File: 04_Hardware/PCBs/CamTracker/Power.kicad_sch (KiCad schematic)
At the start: 95 parts, among them IC2 AP7361E-33FGE-7, IC3 AP7361E-33FGE-7, J1 PJ-059A, J2 67996-100HLF, U1 SC206EEMDA-G51-UGNDA, U15 AP61100Z6-7, U2 AP64502QSP-13, U3 AP7335-WG-7, U6 AP61300Z6-7

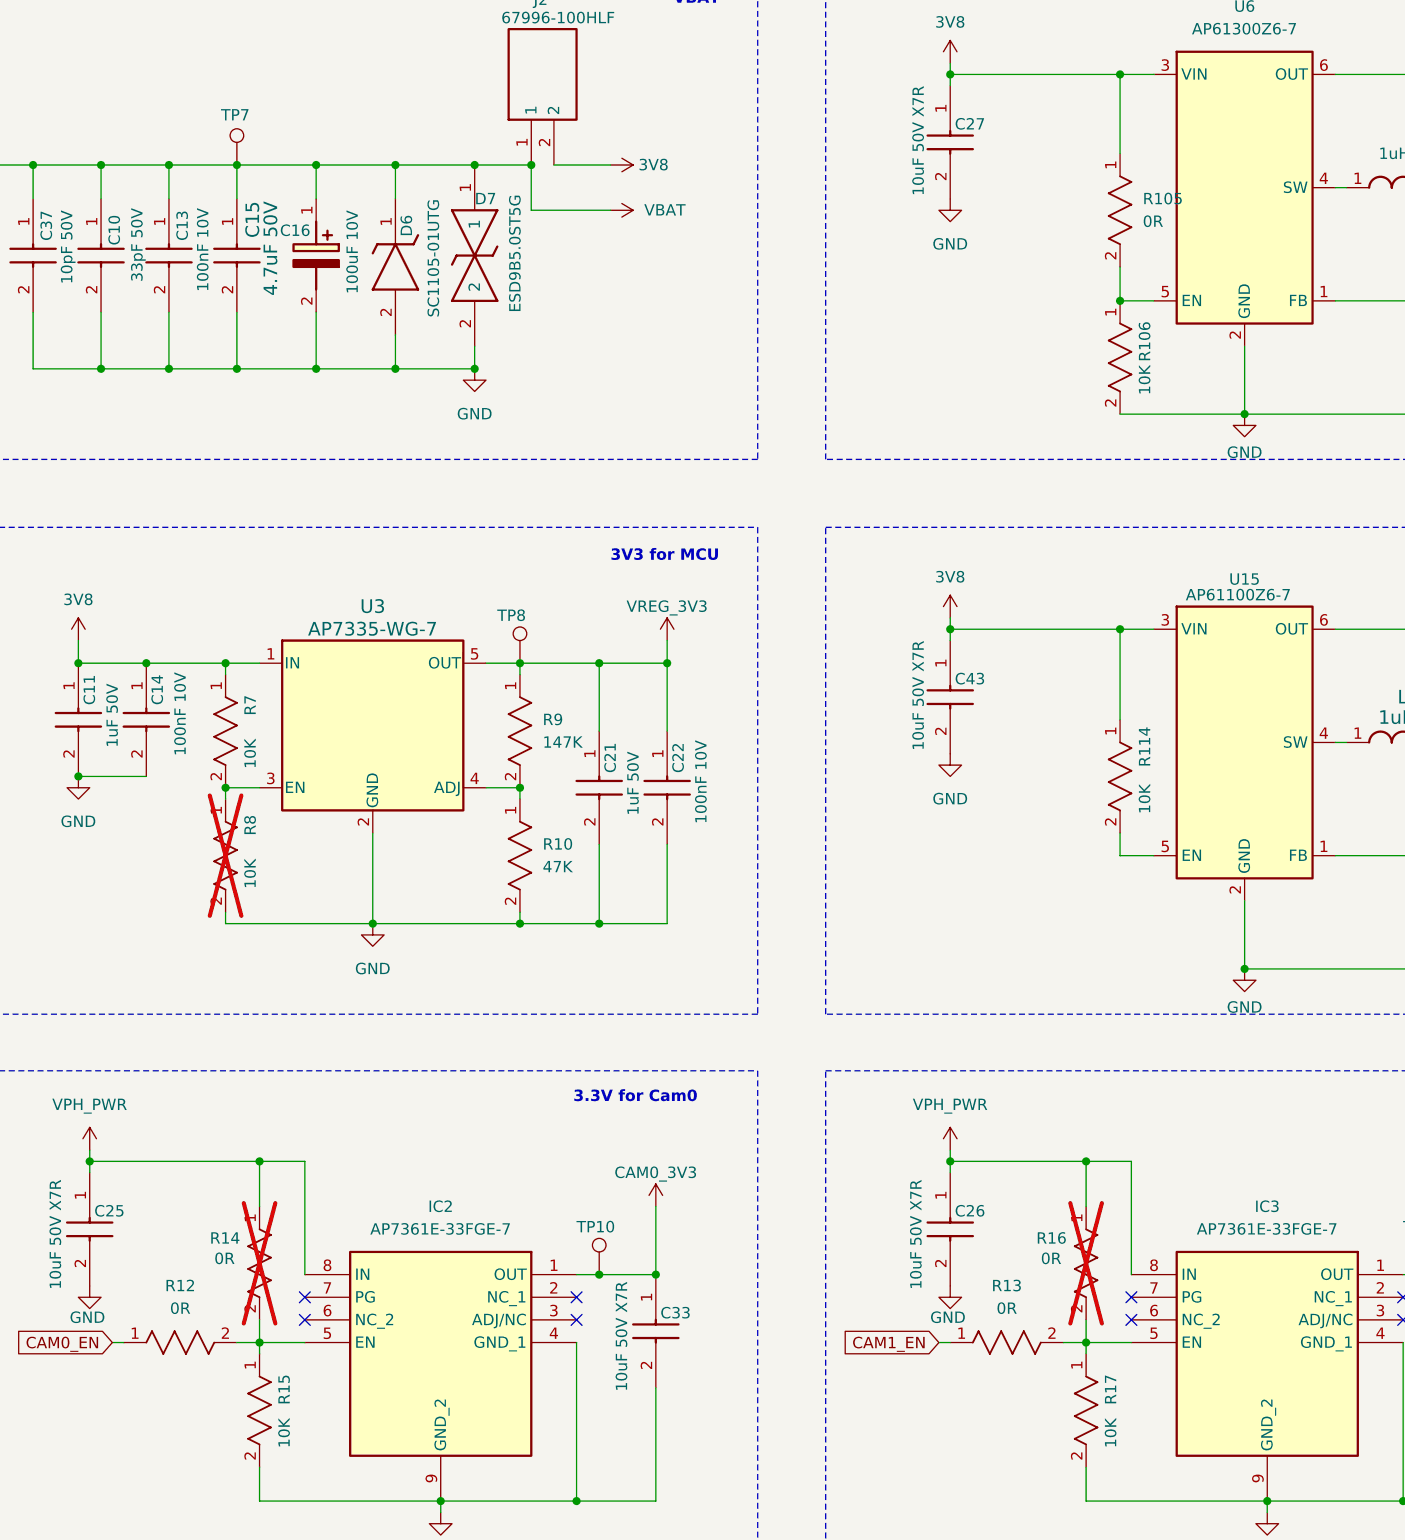
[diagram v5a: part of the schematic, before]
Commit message: feat(PCB): Updated NVME USB EN logic, turn-off the NVME 3V3 and 1V05 by EN pin
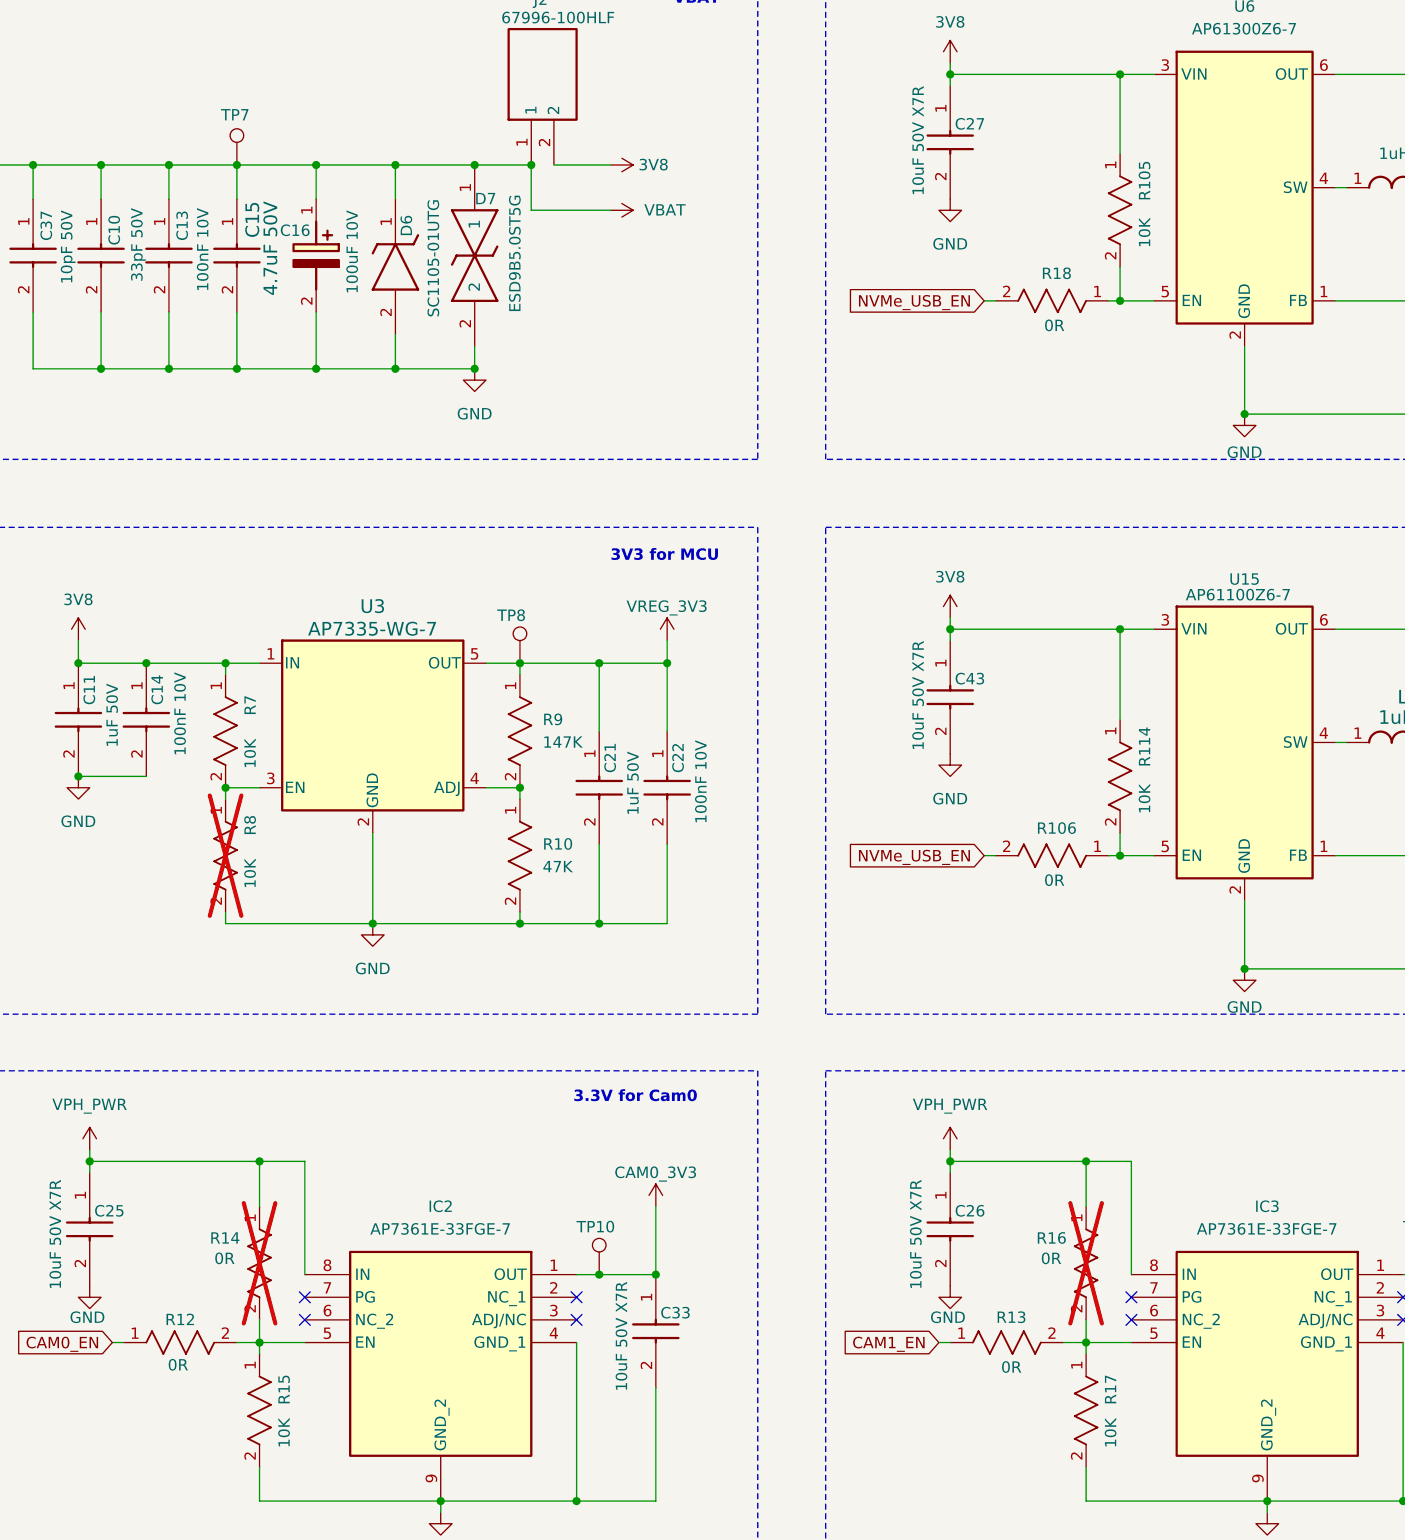
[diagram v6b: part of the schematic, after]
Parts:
- removed R105: 0R, 000MCLib:RESC2012X50N, symbol 000MCLib:CRCW08050000Z0EA
- removed R106: 10K, 000MCLib:RC0402N_YAG, symbol 000MCLib:RC0402JR-0710KL
- added R105: 10K, 000MCLib:RC0402N_YAG, symbol 000MCLib:RC0402JR-0710KL
- added R106, R18: 0R, 000MCLib:RC0402N_YAG, symbol 000MCLib:RC0402JR-070RL
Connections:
- net 3V8: now also R105.1
- net at U6.5 (EN): now also R105.2, R18.1
- net at R114.2, U15.5 (EN): now also R106.1
- new net NVMe_USB_EN: R106.2, R18.2
